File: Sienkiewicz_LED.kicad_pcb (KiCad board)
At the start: 2 copper layers, 38 x 38 mm, 25 parts, among them U1 B-B Interface, U2 STP16CP05M

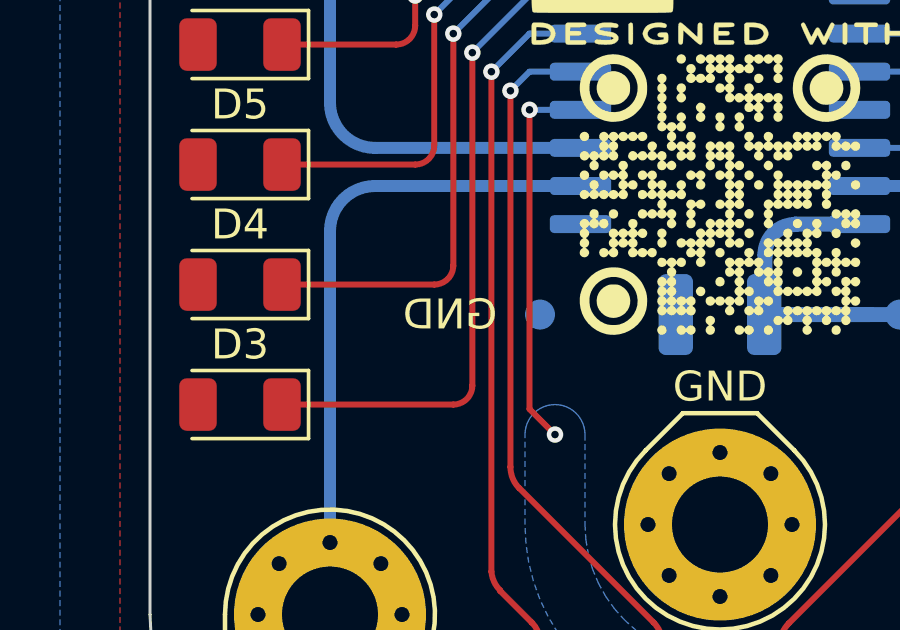
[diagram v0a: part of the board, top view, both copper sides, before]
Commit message: testpoints silkscreen tests
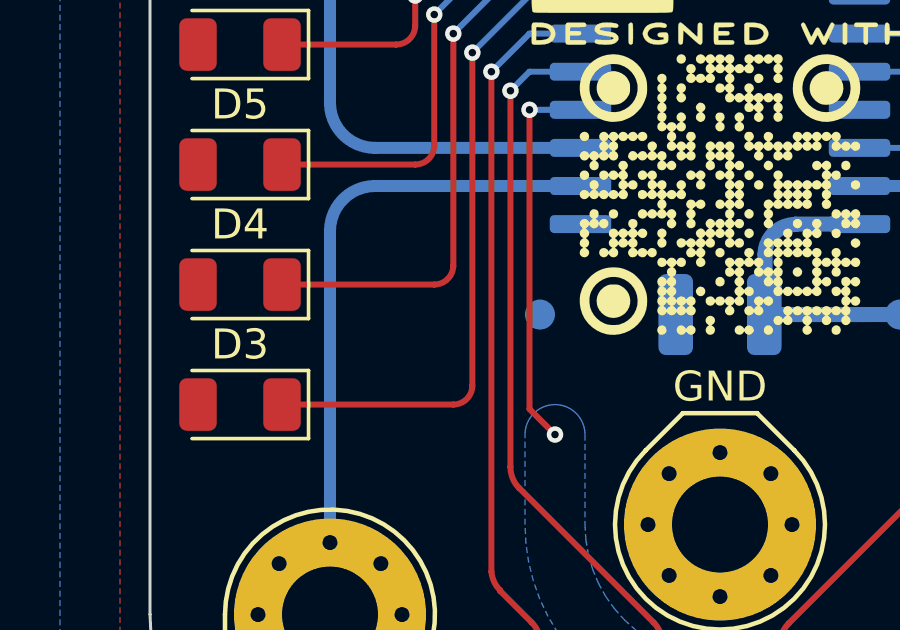
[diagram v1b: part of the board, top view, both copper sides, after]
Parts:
- renumbered TP1 to GND
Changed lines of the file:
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@@
 	(property "DESIGNER" "Paweł Baran")
 	(property "FABRICATION_NOTES" "FABRICATION NOTES (UNLESS OTHERWISE SPECIFIED)\n\n1)	FABRICATE PER IPC-6012A CLASS 2.\n\n2)	OUTLINE DEFINED IN SEPARATE GERBER FILE WITH\n	\"Edge_Cuts.GBR\" SUFFIX.\n\n	DIMENSIONS OF CIRCUMSIZED RECTANGLE SHOWN ON THIS\n	DRAWING FOR REFERENCE ONLY.\n\n3)	SEE SEPARATE DRILL FILES WITH \".DRL\" SUFFIX \n	FOR HOLE LOCATIONS.\n\n	SELECTED HOLE LOCATIONS SHOWN ON THIS DRAWING \n	FOR REFERENCE ONLY.\n\n4)	SURFACE FINISH: IMMERSION GOLD\n\n5)	SOLDERMASK ON BOTH SIDES OF THE BOARD SHALL \n	BE LPI, COLOR BLACK.\n\n6)	SILK SCREEN LEGEND TO BE APPLIED PER LAYER \n	STACKUP USING YELLOW NON-CONDUCTIVE EPOXY INK.\n\n7)	ALL VIAS ARE TENTED ON BOTH SIDES UNLESS \n	SOLDERMASK OPENED IN GERBER.\n\n8)	VENDOR SHOULD FOLLOW ROHS COMPLIANT PROCESS \n	AND Pb FREE FOR MANUFACTURING\n\n9)	PCB MATERIAL REQUIREMENTS:\n\n	A.	FLAMMABILITY RATING MUST MEET OR EXCEED \n		UL94V-0 REQUIREMENTS.\n	B.	Tg 170 C OR EQUIVALENT.\n	C.	EQUIVALENT MATERIAL SHALL BE RoHS COMPLIANT, \n		HALOGEN FREE AND APPROVED BY BAJRAN IMGAGINARY INDUSTRIES.\n\n10)	DESIGN GEOMETRY MINIMUM FEATURE SIZES:\n\n	BOARD SIZE				38.000 × 38.000 mm\n	BOARD THICKNESS		1.660 mm\n	TRACE WIDTH			0.200 mm\n	TRACE TO TRACE		0.200 mm\n	MIN. HOLE (PTH)			0.250 mm\n	MIN. HOLE (NPTH)		N/A mm\n	ANNULAR RING			0.150 mm\n	COPPER TO HOLE		0.254 mm\n	COPPER TO EDGE		0.250 mm\n	HOLE TO HOLE			0.254 mm\n\n11)	REFER TO IMPEDANCE TABLE FOR IMPEDANCE CONTROL REQUIREMENTS.\n\n12)	CONFIRM SPACE WIDTHS AND SPACINGS.")
-	(property "GIT_HASH_PCB" "ec13901")
+	(property "GIT_HASH_PCB" "7dbde01")
 	(property "GIT_HASH_SCH" "8dba9b7")
 	(property "GIT_URL" "https://github.com/nguyen-v/KDT_Hierarchical_KiBot")
@@
 		(descr "SMD pad as test Point, diameter 1.0mm")
 		(tags "test point SMD pad")
-		(property "Reference" "TP1"
-			(at 0 1.448 0)
+		(property "Reference" "GND"
+			(at 3 0 0)
 			(layer "B.SilkS")
-			(hide yes)
 			(effects
 				(font
@@
 		(property "Value" "GND"
 			(at 3 0 0)
-			(layer "F.SilkS")
+			(layer "B.Fab")
+			(hide yes)
 			(effects
 				(font

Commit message: blender rendering silkscreen solved
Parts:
- renumbered TP3 to OE, TP2 to VCC
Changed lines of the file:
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@@
 	(property "DESIGNER" "Paweł Baran")
 	(property "FABRICATION_NOTES" "FABRICATION NOTES (UNLESS OTHERWISE SPECIFIED)\n\n1)	FABRICATE PER IPC-6012A CLASS 2.\n\n2)	OUTLINE DEFINED IN SEPARATE GERBER FILE WITH\n	\"Edge_Cuts.GBR\" SUFFIX.\n\n	DIMENSIONS OF CIRCUMSIZED RECTANGLE SHOWN ON THIS\n	DRAWING FOR REFERENCE ONLY.\n\n3)	SEE SEPARATE DRILL FILES WITH \".DRL\" SUFFIX \n	FOR HOLE LOCATIONS.\n\n	SELECTED HOLE LOCATIONS SHOWN ON THIS DRAWING \n	FOR REFERENCE ONLY.\n\n4)	SURFACE FINISH: IMMERSION GOLD\n\n5)	SOLDERMASK ON BOTH SIDES OF THE BOARD SHALL \n	BE LPI, COLOR BLACK.\n\n6)	SILK SCREEN LEGEND TO BE APPLIED PER LAYER \n	STACKUP USING YELLOW NON-CONDUCTIVE EPOXY INK.\n\n7)	ALL VIAS ARE TENTED ON BOTH SIDES UNLESS \n	SOLDERMASK OPENED IN GERBER.\n\n8)	VENDOR SHOULD FOLLOW ROHS COMPLIANT PROCESS \n	AND Pb FREE FOR MANUFACTURING\n\n9)	PCB MATERIAL REQUIREMENTS:\n\n	A.	FLAMMABILITY RATING MUST MEET OR EXCEED \n		UL94V-0 REQUIREMENTS.\n	B.	Tg 170 C OR EQUIVALENT.\n	C.	EQUIVALENT MATERIAL SHALL BE RoHS COMPLIANT, \n		HALOGEN FREE AND APPROVED BY BAJRAN IMGAGINARY INDUSTRIES.\n\n10)	DESIGN GEOMETRY MINIMUM FEATURE SIZES:\n\n	BOARD SIZE				38.000 × 38.000 mm\n	BOARD THICKNESS		1.660 mm\n	TRACE WIDTH			0.200 mm\n	TRACE TO TRACE		0.200 mm\n	MIN. HOLE (PTH)			0.250 mm\n	MIN. HOLE (NPTH)		N/A mm\n	ANNULAR RING			0.150 mm\n	COPPER TO HOLE		0.254 mm\n	COPPER TO EDGE		0.250 mm\n	HOLE TO HOLE			0.254 mm\n\n11)	REFER TO IMPEDANCE TABLE FOR IMPEDANCE CONTROL REQUIREMENTS.\n\n12)	CONFIRM SPACE WIDTHS AND SPACINGS.")
-	(property "GIT_HASH_PCB" "7dbde01")
+	(property "GIT_HASH_PCB" "e0292db")
 	(property "GIT_HASH_SCH" "8dba9b7")
 	(property "GIT_URL" "https://github.com/nguyen-v/KDT_Hierarchical_KiBot")
@@
 		(descr "SMD pad as test Point, diameter 1.0mm")
 		(tags "test point SMD pad")
-		(property "Reference" "TP2"
-			(at 0 1.448 0)
+		(property "Reference" "VCC"
+			(at -3 0 0)
 			(layer "B.SilkS")
-			(hide yes)
 			(effects
 				(font
@@
 		(property "Value" "VCC"
 			(at -3 0 0)
-			(layer "B.SilkS")
+			(layer "B.Fab")
+			(hide yes)
 			(effects
 				(font
@@
 		(descr "SMD pad as test Point, diameter 1.0mm")
 		(tags "test point SMD pad")
-		(property "Reference" "TP3"
-			(at 0 1.448001 90)
+		(property "Reference" "OE"
+			(at 0 3.84 0)
 			(layer "B.SilkS")
-			(hide yes)
 			(effects
 				(font
@@
 		(property "Value" "OE"
 			(at 0 3.81 0)
-			(layer "B.SilkS")
+			(layer "B.Fab")
+			(hide yes)
 			(effects
 				(font

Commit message: Update Outputs (release)
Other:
- board text added: "0.02mm"
- board text added: "0.07mm (2.00oz)"
- board text added: "1.48mm"
- board text added: "B.Cu (Sig, PWR)"
- board text added: "B.Mask"
- board text added: "B.Paste"
- board text added: "B.Silkscreen"
- board text added: "Copper"
- board text added: "Core"
- board text added: "Dielectric"
- board text added: "Direct Printing"
- board text added: "F.Mask"
- board text added: "F.Paste"
- board text added: "F.Silkscreen"
- board text added: "FR4_7628"
- board text added: "GBR"
- board text added: "Gerber"
- board text added: "Layer"
- board text added: "Legend"
- board text added: "Material"
- board text added: "Note: external layer thicknesses are specified after plating"
- board text added: "Paste Mask"
- board text added: "Signal"
- board text added: "Solder Mask"
- board text added: "Solder Resist"
- board text added: "T.Cu (Sig, PWR)"
- board text added: "Thickness"
- board text added: "Total thickness: 1.66mm"
- board text added: "Type"

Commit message: documentation update / block diagram
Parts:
- TP1: renamed from GND; value GND -> TestPoint
- TP2: renamed from VCC; value VCC -> TestPoint
- TP3: renamed from OE; value OE -> TestPoint
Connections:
- D1 pad 1: /Project Architecture/Sec B - Shift Register/L1 -> /Project Architecture/Sec C - LED Display/L1
- D10 pad 1: /Project Architecture/Sec B - Shift Register/L10 -> /Project Architecture/Sec C - LED Display/L10
- D11 pad 1: /Project Architecture/Sec B - Shift Register/L11 -> /Project Architecture/Sec C - LED Display/L11
- D12 pad 1: /Project Architecture/Sec B - Shift Register/L12 -> /Project Architecture/Sec C - LED Display/L12
- D13 pad 1: /Project Architecture/Sec B - Shift Register/L13 -> /Project Architecture/Sec C - LED Display/L13
- D14 pad 1: /Project Architecture/Sec B - Shift Register/L14 -> /Project Architecture/Sec C - LED Display/L14
- D15 pad 1: /Project Architecture/Sec B - Shift Register/L15 -> /Project Architecture/Sec C - LED Display/L15
- D16 pad 1: /Project Architecture/Sec B - Shift Register/L16 -> /Project Architecture/Sec C - LED Display/L16
- D2 pad 1: /Project Architecture/Sec B - Shift Register/L2 -> /Project Architecture/Sec C - LED Display/L2
- D3 pad 1: /Project Architecture/Sec B - Shift Register/L3 -> /Project Architecture/Sec C - LED Display/L3
- D4 pad 1: /Project Architecture/Sec B - Shift Register/L4 -> /Project Architecture/Sec C - LED Display/L4
- D5 pad 1: /Project Architecture/Sec B - Shift Register/L5 -> /Project Architecture/Sec C - LED Display/L5
- D6 pad 1: /Project Architecture/Sec B - Shift Register/L6 -> /Project Architecture/Sec C - LED Display/L6
- D7 pad 1: /Project Architecture/Sec B - Shift Register/L7 -> /Project Architecture/Sec C - LED Display/L7
- D8 pad 1: /Project Architecture/Sec B - Shift Register/L8 -> /Project Architecture/Sec C - LED Display/L8
- D9 pad 1: /Project Architecture/Sec B - Shift Register/L9 -> /Project Architecture/Sec C - LED Display/L9
- U2 pad 2: /Project Architecture/Sec A - Shift Register Screw Interface/SR_CLK -> /Project Architecture/Sec B - Shift Register/RS_SDI
- U2 pad 3: /Project Architecture/Sec A - Shift Register Screw Interface/SR_SDI -> /Project Architecture/Sec B - Shift Register/RS_CLK
- U2 pad 4: /Project Architecture/Sec A - Shift Register Screw Interface/SR_LATCH -> /Project Architecture/Sec B - Shift Register/RS_LATCH
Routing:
- net /Project Architecture/Sec B - Shift Register/RS_LATCH: track 0.00 -> 12.9 mm, vias 0 -> 1
- net /Project Architecture/Sec A - Shift Register Screw Interface/SR_LATCH: track 12.9 -> 0.00 mm, vias 2 -> 1

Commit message: documentation update / release 2.1.1 prep
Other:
- board text removed: "30°"
- board text removed: "3× 120°"
